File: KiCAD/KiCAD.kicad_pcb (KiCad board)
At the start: 2 copper layers, 112.1 x 150 mm, 142 parts, among them J1 Conn_01x02_Pin, J13 Conn_01x05, J15 Conn_01x03_Pin, J16 Conn_01x05, J4 8P8C_Shielded, J5 ENC_INT if needed, J6 TX/RX, J7 HV, J8 HV_INRUSH_BYPASS, J9 TR_SENSE, Q1 J310, Q4 2N7000, Q5 2N7000, Q6 2N7000, Q7 2N7000, T1 2N3906, T2 2N3906, U1 Si5351A_Breakout, U15 LM7805_TO220, U16 AM26LS32ACN, U17 Adafruit_PCF8575_Breakout, U18 CD14538B, U19 L79L08_TO92, U20 ICL7660S, U3 MC1496, U4 MCP4921, U6 LM7171xIN, U7 LM7171xIN, U8 MCP4728

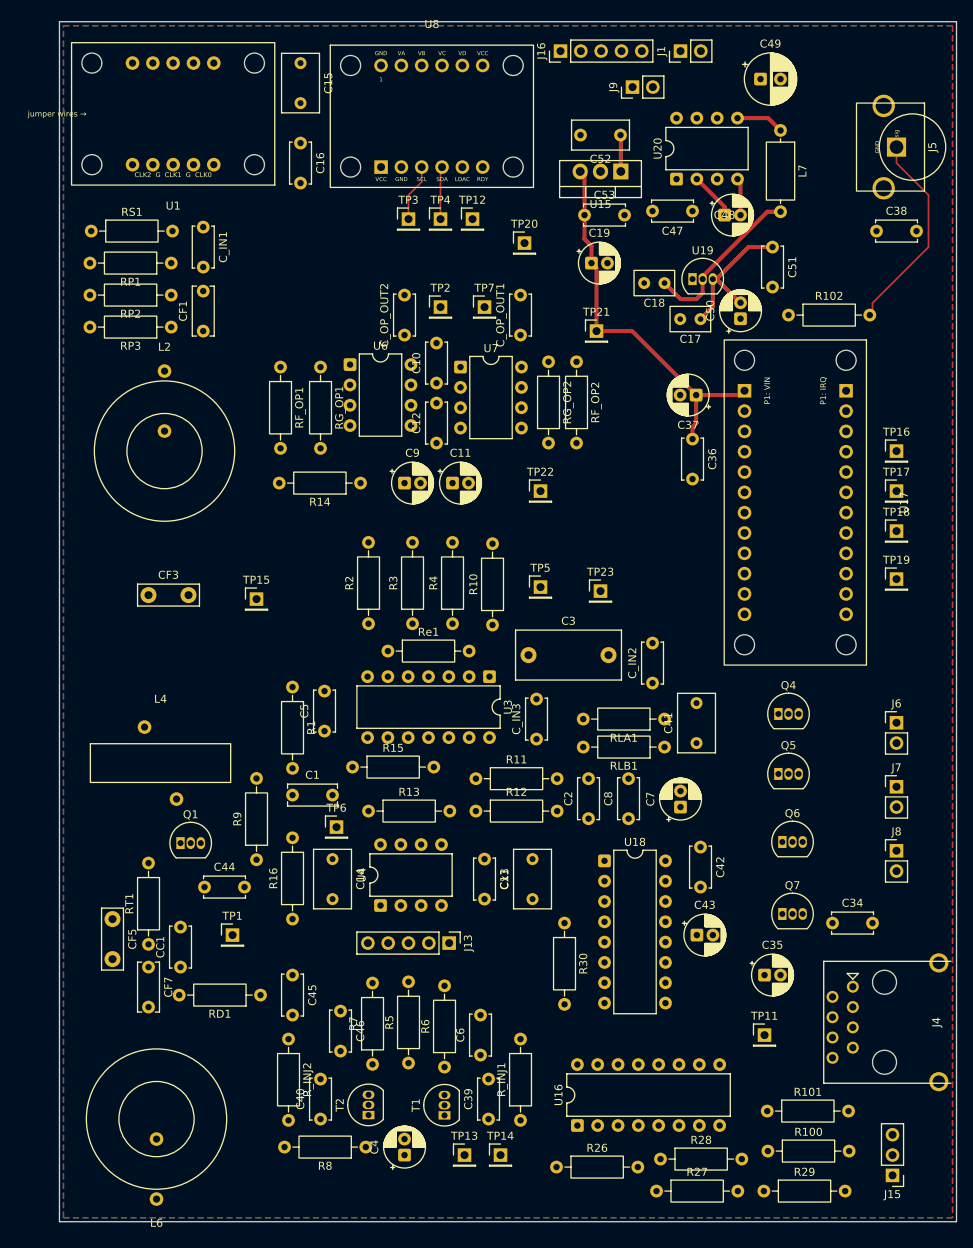
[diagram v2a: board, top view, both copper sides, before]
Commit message: kicad: fix GND zone net (was +12V); more routing progress
- Both GND zones on F.Cu and B.Cu had (net "+12V") in the zone
  definition, so pour was filling the wrong net and every GND pad
  showed as unconnected. Corrected to (net "GND").
- Additional routing and placement adjustments on buffer_keyer

Co-Authored-By: Claude Opus 4.7 <noreply@anthropic.com>
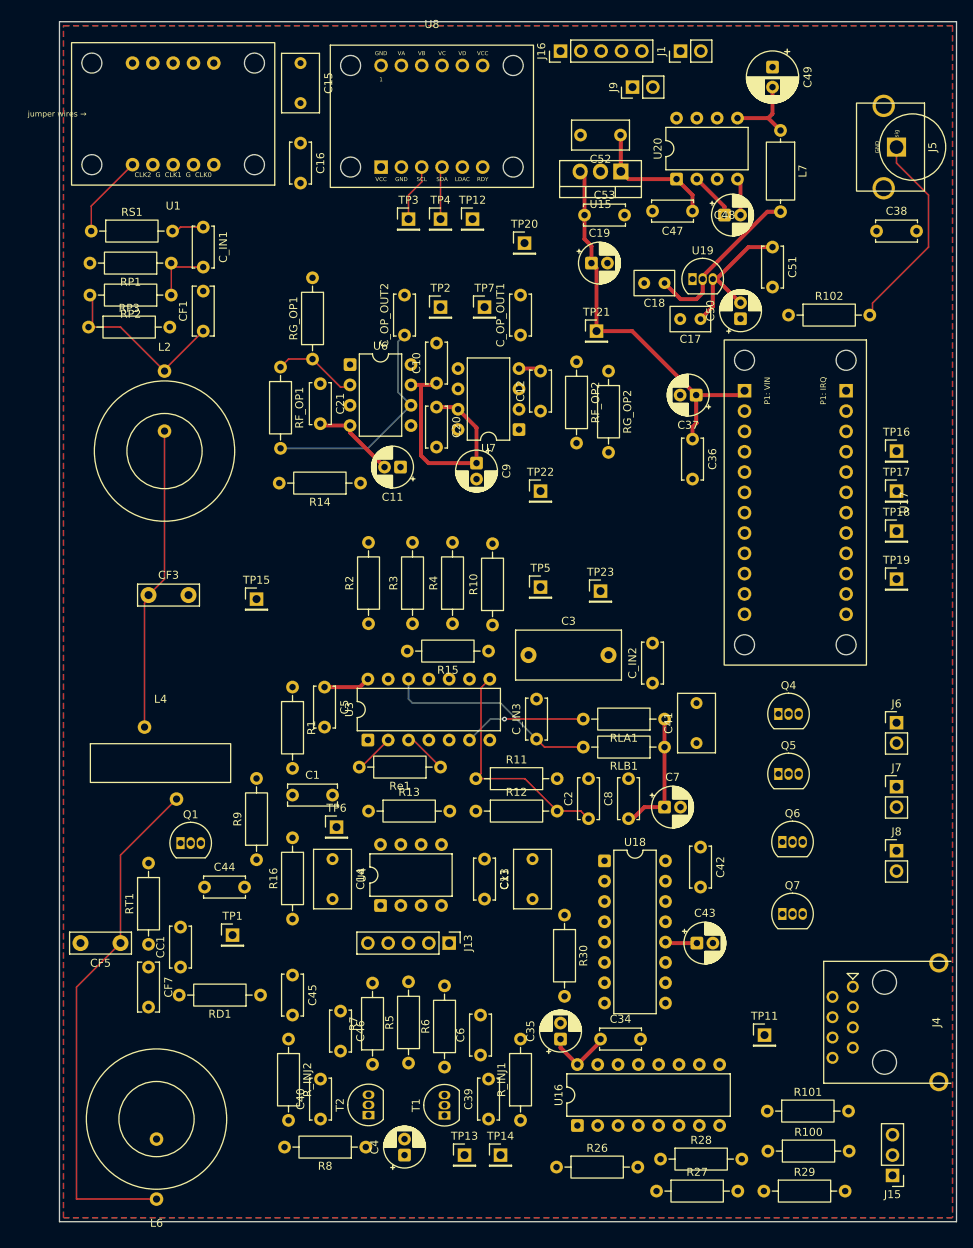
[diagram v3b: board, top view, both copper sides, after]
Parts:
- added C20: 100nF, Capacitor_THT:C_Disc_D5.0mm_W2.5mm_P5.00mm, F.Cu at (63.0, 62.5)
- added C21: 100nF, Capacitor_THT:C_Disc_D5.0mm_W2.5mm_P5.00mm, F.Cu at (48.5, 59.6)
- moved C34 32.4 mm to (83.5, 141.5)
- moved C35 26.7 mm to (78.5, 141.5), turned to 90 degrees
- moved R15 22.3 mm to (69.5, 93.0), turned to 180 degrees
- moved U3 17.1 mm to (54.4, 104.1), turned to 90 degrees
- moved Re1 15.9 mm to (63.5, 107.5), turned to 180 degrees
- moved C12 13.6 mm to (76.0, 63.0)
- moved U7 10.7 mm to (73.3, 65.3), turned to 180 degrees
- moved RP3 10.3 mm to (19.5, 52.5), turned to 0 degrees
- moved C9 9.34 mm to (68.0, 69.5), turned to -90 degrees
- moved RG_OP2 7.59 mm to (84.5, 58.0)
- moved C11 6.80 mm to (58.5, 70.0), turned to 180 degrees
- moved C5 5.50 mm to (49.0, 97.5), turned to -90 degrees
- moved CF5 3.16 mm to (23.5, 129.5), turned to 180 degrees
- moved C49 2.12 mm to (105.0, 20.0), turned to -90 degrees
- moved C7 2.00 mm to (91.5, 112.5), turned to 0 degrees
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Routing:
- net Net-(CF5-Pad1): track 0.00 -> 65.2 mm
- net +12V: track 4.57 -> 63.5 mm
- net Net-(CF3-Pad1): track 0.00 -> 38.0 mm
- net Net-(U3-CAR_IN-): track 0.00 -> 29.3 mm
- net DRV_OUT+: track 0.00 -> 28.3 mm
- net MC_OUT-: track 0.00 -> 26.8 mm
- net Net-(CF1-Pad1): track 0.00 -> 23.3 mm
- net VEE: track 19.1 -> 39.0 mm
- net MC_OUT+: track 0.00 -> 15.3 mm, vias 0 -> 1
- net +5V: track 48.7 -> 61.1 mm
- net Net-(U6--): track 0.00 -> 10.7 mm
- net Net-(RS1-Pad1): track 0.00 -> 10.4 mm
- net Net-(C_IN1-Pad2): track 0.00 -> 8.21 mm
- net Net-(U3-GADJ_B): track 0.00 -> 5.40 mm
- net Net-(U3-GADJ_A): track 0.00 -> 5.02 mm
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
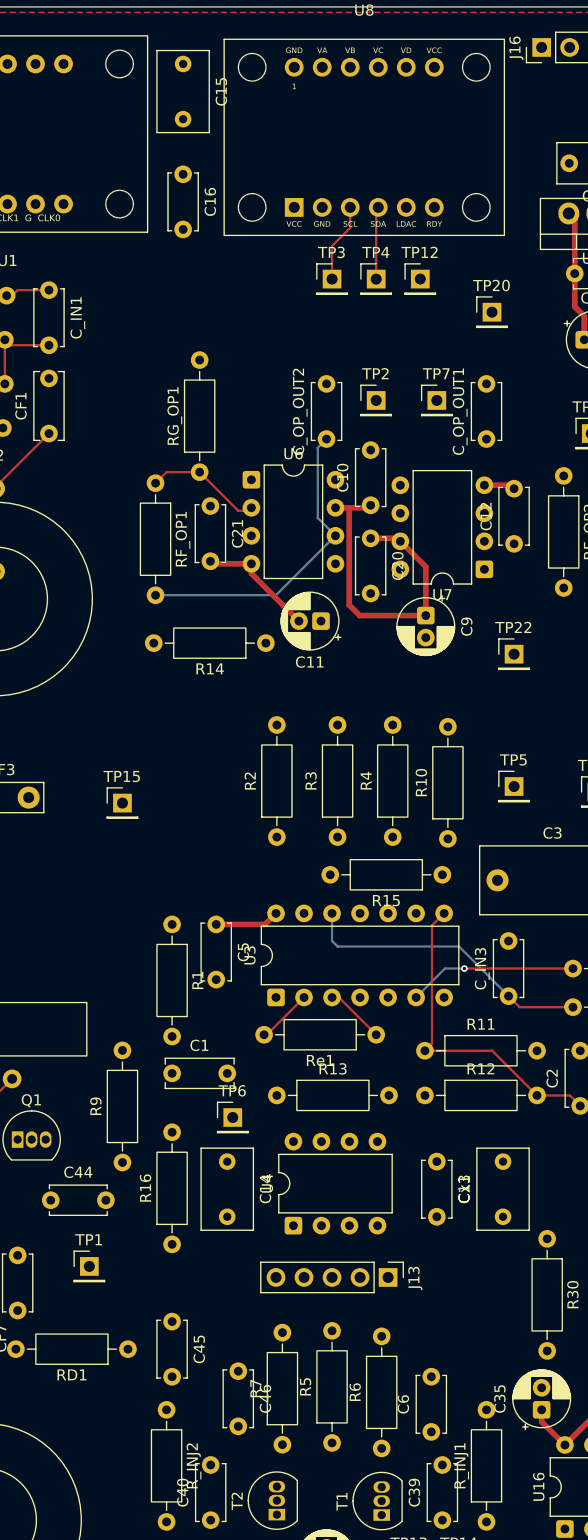
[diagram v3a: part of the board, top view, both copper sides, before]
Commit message: kicad: routing progress + VA/VB filter caps + LM7805 bulk cap
- Add 100nF filter caps at R_INJ inputs (VA/VB) to block long-trace
  RF pickup at MC1496 carrier-null network
- Add 10uF bulk cap at LM7805 output (C35 too far to serve this role)
- More traces routed on buffer_keyer, some VA/VB routing on B.Cu to
  clear L2/L4 toroid area

Co-Authored-By: Claude Opus 4.7 <noreply@anthropic.com>
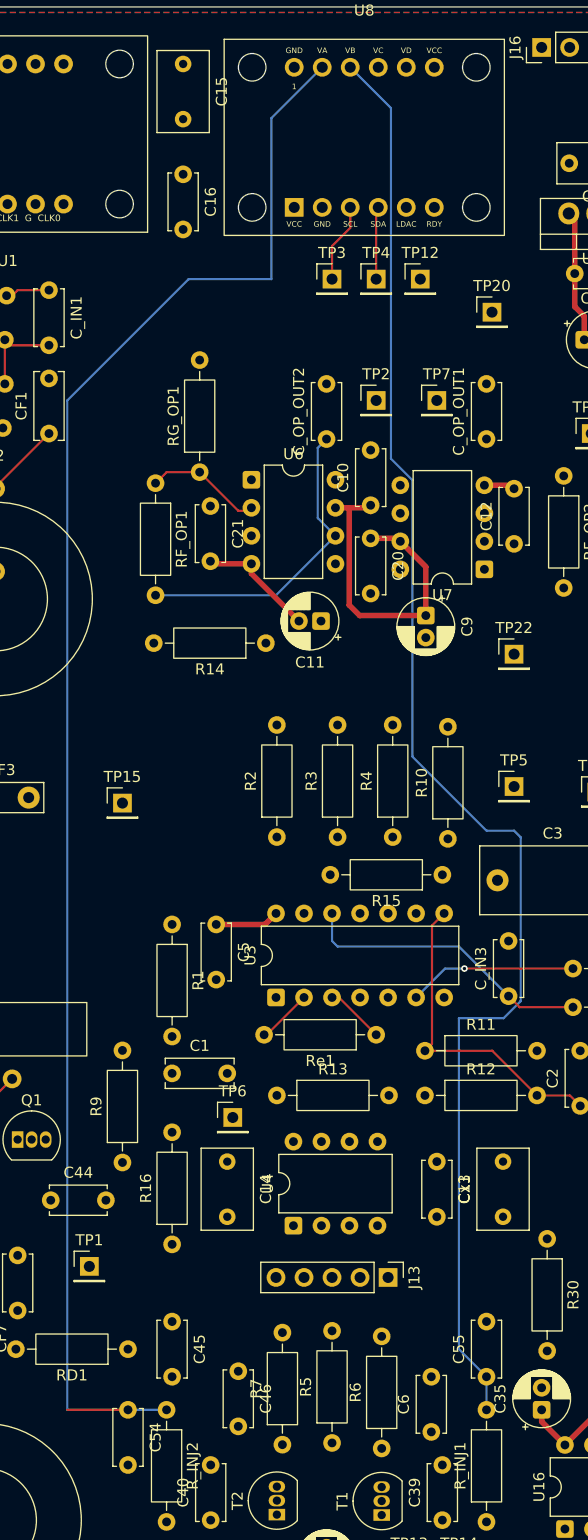
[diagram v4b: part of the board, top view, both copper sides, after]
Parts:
- added C54: 100nF, Capacitor_THT:C_Disc_D5.0mm_W2.5mm_P5.00mm, F.Cu at (41.0, 141.5)
- added C55: 100nF, Capacitor_THT:C_Disc_D5.0mm_W2.5mm_P5.00mm, F.Cu at (73.5, 138.5)
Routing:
- net VA_INJ: track 0.00 -> 150.2 mm
- net VB_INJ: track 0.00 -> 135.3 mm

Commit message: kicad: additional routing progress on buffer_keyer PCB
Co-Authored-By: Claude Opus 4.7 <noreply@anthropic.com>
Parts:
- moved C38 30.4 mm to (93.8, 22.2)
- moved TP22 28.6 mm to (55.5, 93.0)
- moved C41 20.9 mm to (80.0, 118.5), turned to -90 degrees
- moved TP20 11.4 mm to (77.0, 53.0)
- moved TP11 9.34 mm to (106.5, 132.0)
- moved R8 6.61 mm to (59.0, 159.5)
- moved C1 5.00 mm to (50.0, 111.0), turned to 180 degrees
- moved TP1 4.61 mm to (41.0, 131.5)
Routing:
- net 3V3: track 0.00 -> 240.5 mm
- net SDA: track 6.58 -> 222.1 mm
- net SCL: track 7.18 -> 156.7 mm, vias 0 -> 1
- net +5V: track 61.1 -> 186.3 mm
- net +12V: track 63.5 -> 184.9 mm, vias 0 -> 1
- net T1_COL: track 0.00 -> 89.8 mm
- net Net-(U3-SIG_IN+): track 0.00 -> 82.0 mm, vias 0 -> 3
- net Net-(U18-+TR_A): track 0.00 -> 73.7 mm
- net Net-(U6-+): track 0.00 -> 70.6 mm, vias 0 -> 1
- net VEE: track 39.0 -> 107.7 mm, vias 0 -> 3
- net T2_COL: track 0.00 -> 57.0 mm
- net Net-(Q6-G): track 0.00 -> 53.2 mm
- net Net-(Q5-G): track 0.00 -> 44.5 mm
- net Net-(U7-+): track 0.00 -> 42.9 mm
- net Net-(Q4-G): track 0.00 -> 40.6 mm
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
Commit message: kicad: further routing progress on buffer_keyer PCB
Co-Authored-By: Claude Opus 4.7 <noreply@anthropic.com>
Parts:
- moved TP23 18.0 mm to (95.8, 98.8)
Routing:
- net +12V: track 184.9 -> 335.4 mm, vias 1 -> 2
- net VEE: track 107.7 -> 197.0 mm
- net Net-(U3-CAR_IN-): track 29.3 -> 86.3 mm
- net MBL_A_P: track 0.00 -> 53.6 mm
- net MBL_A_N: track 0.00 -> 47.3 mm
- net MBL600_A: track 0.00 -> 34.8 mm
- net Net-(CC1-Pad1): track 0.00 -> 29.0 mm
- net MBL_B_N: track 0.00 -> 27.6 mm
- net MBL_B_P: track 0.00 -> 25.9 mm
- net MBL600_B: track 0.00 -> 21.2 mm
- net MC_OUT+: track 15.3 -> 32.3 mm
- net Net-(U16-2Y): track 0.00 -> 9.98 mm
- net Net-(U16-1Y): track 0.00 -> 6.28 mm
- net Net-(U3-SIG_IN+): vias 3 -> 2

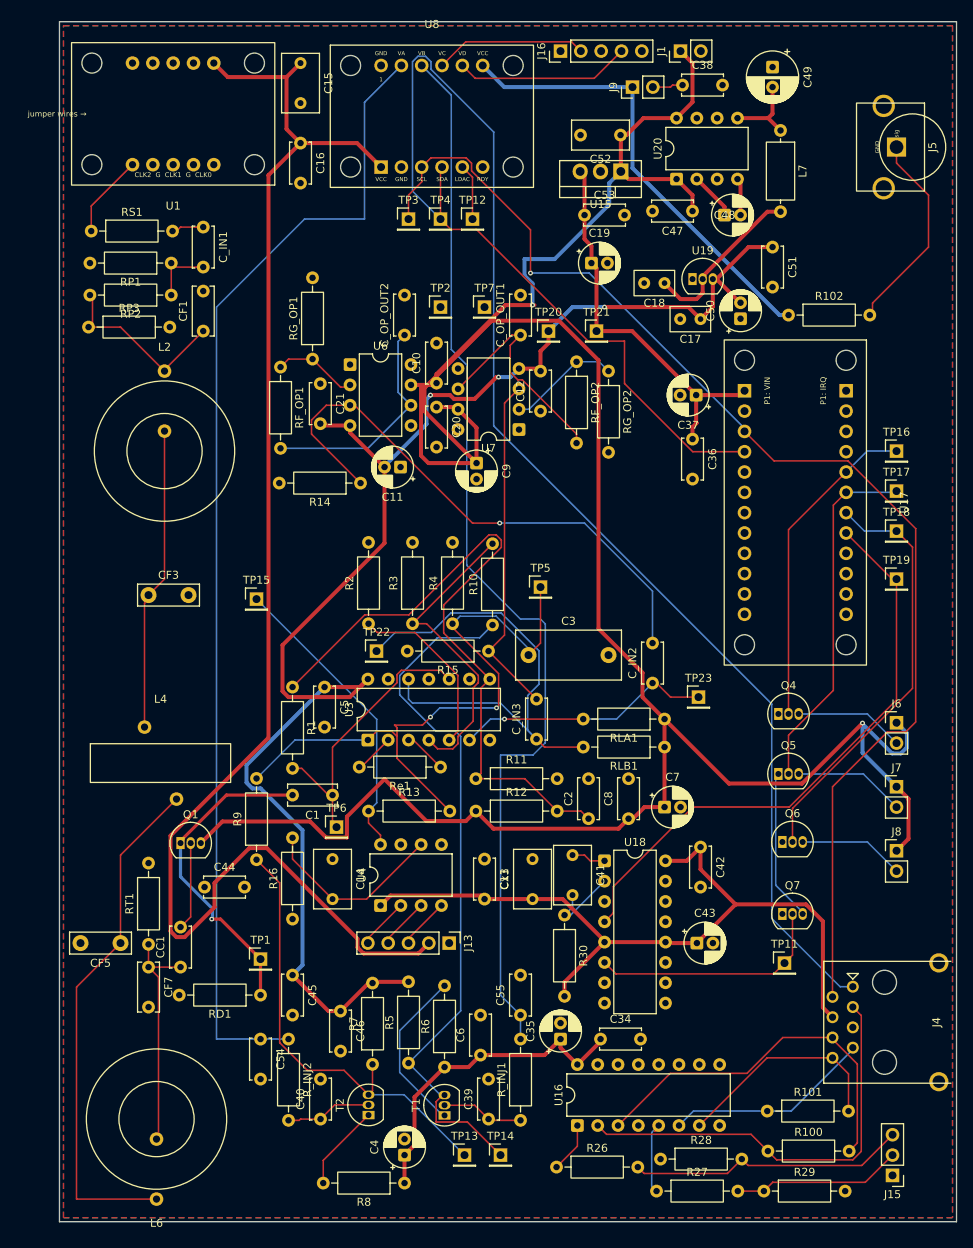
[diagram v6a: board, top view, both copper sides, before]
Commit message: kicad: fix L7 to Device:L symbol, add JFET gate leak on VFO
- buffer_keyer.kicad_sch: L7 (22uH choke) now uses Device:L symbol
  instead of Device:R. Netlist and footprint unchanged; symbol now
  renders as inductor loops instead of resistor rectangle.
- vfo.kicad_sch + PCB: added 10K gate-leak resistor at Q1 (J310 buffer)
  to provide DC gate reference. Was missing from KiCad implementation
  but present in QUCS reference schematic as RGL 1M (10K is fine).
- 5 initial mounting holes placed on PCB (positions will be reworked in
  the next commit).

Co-Authored-By: Claude Opus 4.7 <noreply@anthropic.com>
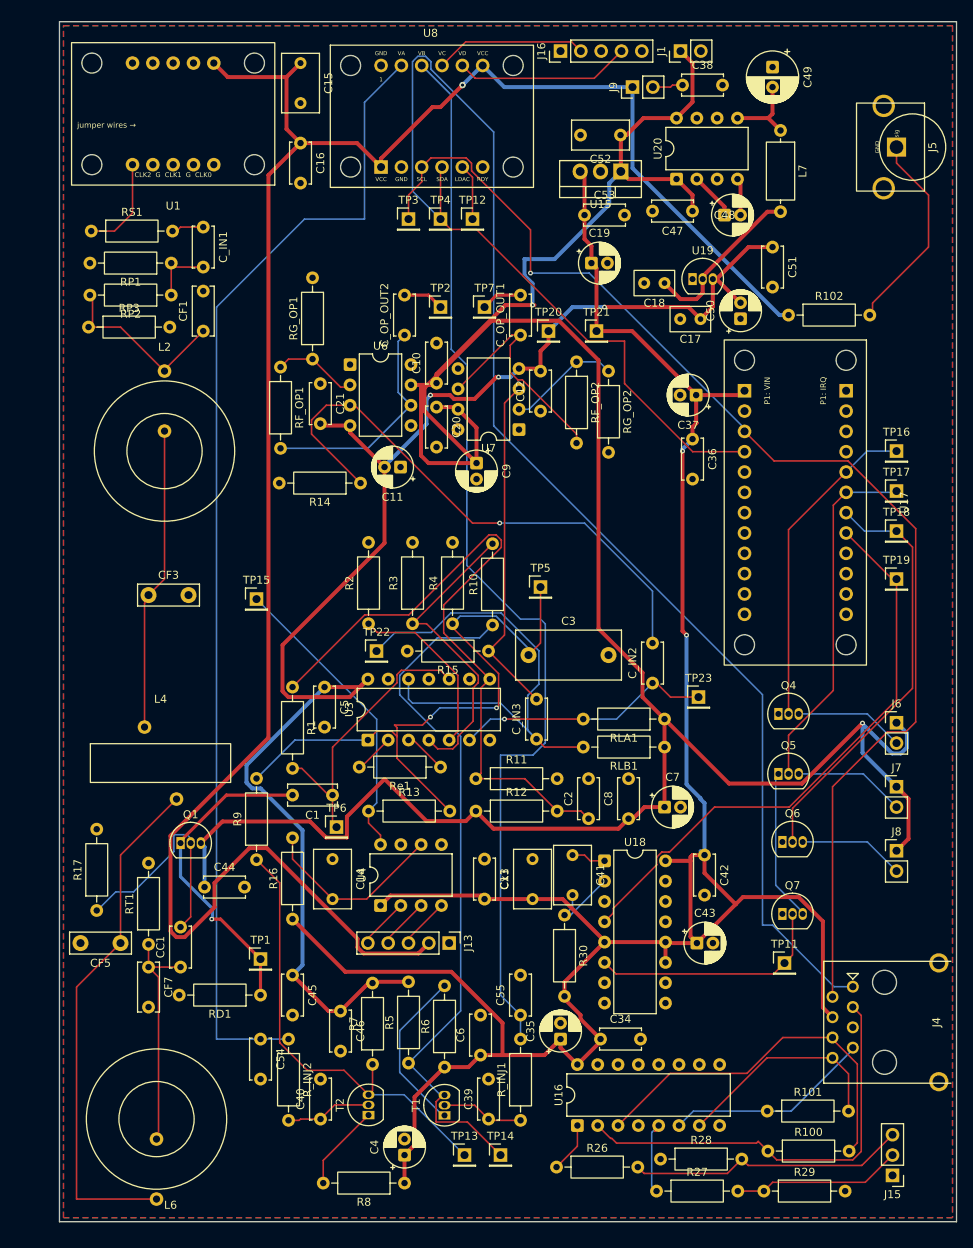
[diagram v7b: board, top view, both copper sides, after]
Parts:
- added R17: 10K, Resistor_THT:R_Axial_DIN0207_L6.3mm_D2.5mm_P10.16mm_Horizontal, F.Cu at (20.5, 125.4)
- moved C42 1.12 mm to (96.5, 118.5)
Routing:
- net +5V: track 186.3 -> 296.9 mm, vias 0 -> 2
- net 3V3: track 240.5 -> 259.1 mm, vias 0 -> 1
- net Net-(Q1-G): track 11.0 -> 28.7 mm
- net +12V: track 335.4 -> 341.1 mm
- net MOD_RF_OUT-: track 0.00 -> 5.12 mm
- net MOD_RF_OUT+: track 0.00 -> 5.12 mm
- net Net-(RS1-Pad1): track 10.4 -> 12.1 mm
- net SDA: track 222.1 -> 223.3 mm
- net Net-(U18-+TR_A): track 73.7 -> 72.7 mm
